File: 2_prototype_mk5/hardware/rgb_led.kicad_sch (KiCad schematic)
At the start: 2 parts

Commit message: MKV revision 1
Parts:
- removed C27: 0.1uF, Capacitor_SMD:C_0603_1608Metric, symbol Device:C
- removed D4: WS2812B, LED_SMD:LED_WS2812B_PLCC4_5.0x5.0mm_P3.2mm, symbol LED:WS2812B
- added LED1: XL-3528RGBW-HM, Custom:LED-SMD_4P-L3.2-W2.8-LS3.5-XL-3528RGBW-HM5, symbol Project symbols:XL-3528RGBW-HM
- added R18: 56R, Resistor_SMD:R_0402_1005Metric, symbol Device:R
- added R19: 270R, Resistor_SMD:R_0402_1005Metric, symbol Device:R
- added R20: 33R, Resistor_SMD:R_0402_1005Metric, symbol Device:R
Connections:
- new net: LED1.3 (G-), R18.2
- new net: LED1.1 (R-), R19.2
- new net: LED1.4 (B-), R20.2
- new net +3V3: LED1.2 (+)
- new net RGB_LED_BLUE: R20.1
- new net RGB_LED_GREEN: R18.1
- new net RGB_LED_RED: R19.1
- no-connect marks 1 -> 0
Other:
- note added: "Common anode RGB LED"
- note added: "https://www.lcsc.com/product-detail/C2843813.html?s_z=n_q_C2843813&globalKeyword=C2843813"
- note removed: "Neopixels addressable RBG LED"
- note removed: "Used for daisy chaining multiple LEDs"

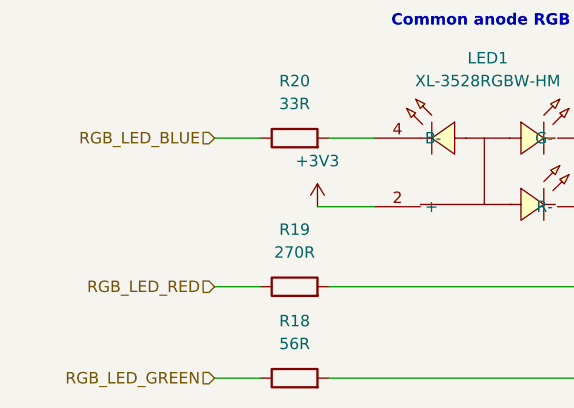
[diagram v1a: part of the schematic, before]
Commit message: Cost reductions for JCLPCB
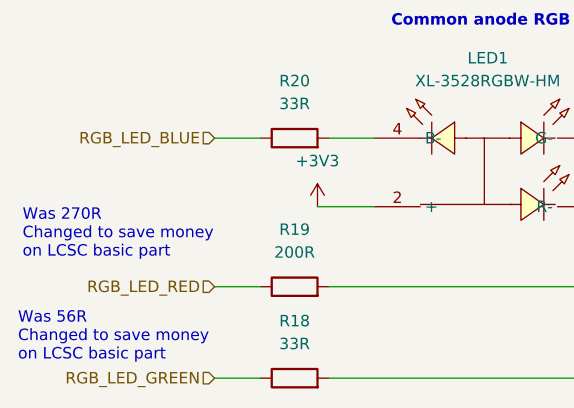
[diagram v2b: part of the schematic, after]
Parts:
- R18: value 56R -> 33R; LCSC Part Number C25173 -> C25105
- R19: value 270R -> 200R; LCSC Part Number C137892 -> C25087
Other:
- note added: "Was 270R Changed to save money on LCSC basic part"
- note added: "Was 56R Changed to save money on LCSC basic part"
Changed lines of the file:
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@@
 	(generator_version "10.0")
 	(paper "A4")
+	(text "Was 270R\nChanged to save money\non LCSC basic part"
+		(exclude_from_sim no)
+		(at 81.534 123.698 0)
+		(effects
+			(font
+				(size 1.27 1.27)
+			)
+			(justify left)
+		)
+	)
 	(text "https://www.lcsc.com/product-detail/C2843813.html?s_z=n_q_C2843813&globalKeyword=C2843813"
 		(exclude_from_sim no)
@@
 				(bold yes)
 			)
+		)
+	)
+	(text "Was 56R\nChanged to save money\non LCSC basic part"
+		(exclude_from_sim no)
+		(at 81.026 135.128 0)
+		(effects
+			(font
+				(size 1.27 1.27)
+			)
+			(justify left)
 		)
 	)
@@
 			)
 		)
-		(property "Value" "56R"
+		(property "Value" "33R"
 			(at 111.76 135.89 90)
 			(show_name no)
@@
 			)
 		)
-		(property "LCSC Part Number" "C25173"
+		(property "LCSC Part Number" "C25105"
 			(at 111.76 139.7 0)
 			(hide yes)
@@
 			)
 		)
-		(property "Value" "270R"
+		(property "Value" "200R"
 			(at 111.76 125.73 90)
 			(show_name no)
@@
 			)
 		)
-		(property "LCSC Part Number" "C137892"
-			(at 111.76 129.54 0)
-			(hide yes)
+		(property "LCSC Part Number" "C25087"
+			(at 111.76 129.54 0)
+			(hide yes)

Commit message: 5.3.0 sent to JCLPCB
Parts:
- LED1: LCSC Part C2843813 -> (none)
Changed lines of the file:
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@@
 			)
 		)
-		(property "LCSC Part" "C2843813"
+		(property "LCSC Part" ""
 			(at 133.35 138.43 0)
 			(hide yes)
